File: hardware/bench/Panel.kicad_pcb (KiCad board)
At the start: 4 copper layers, 151 x 139 mm, 390 parts

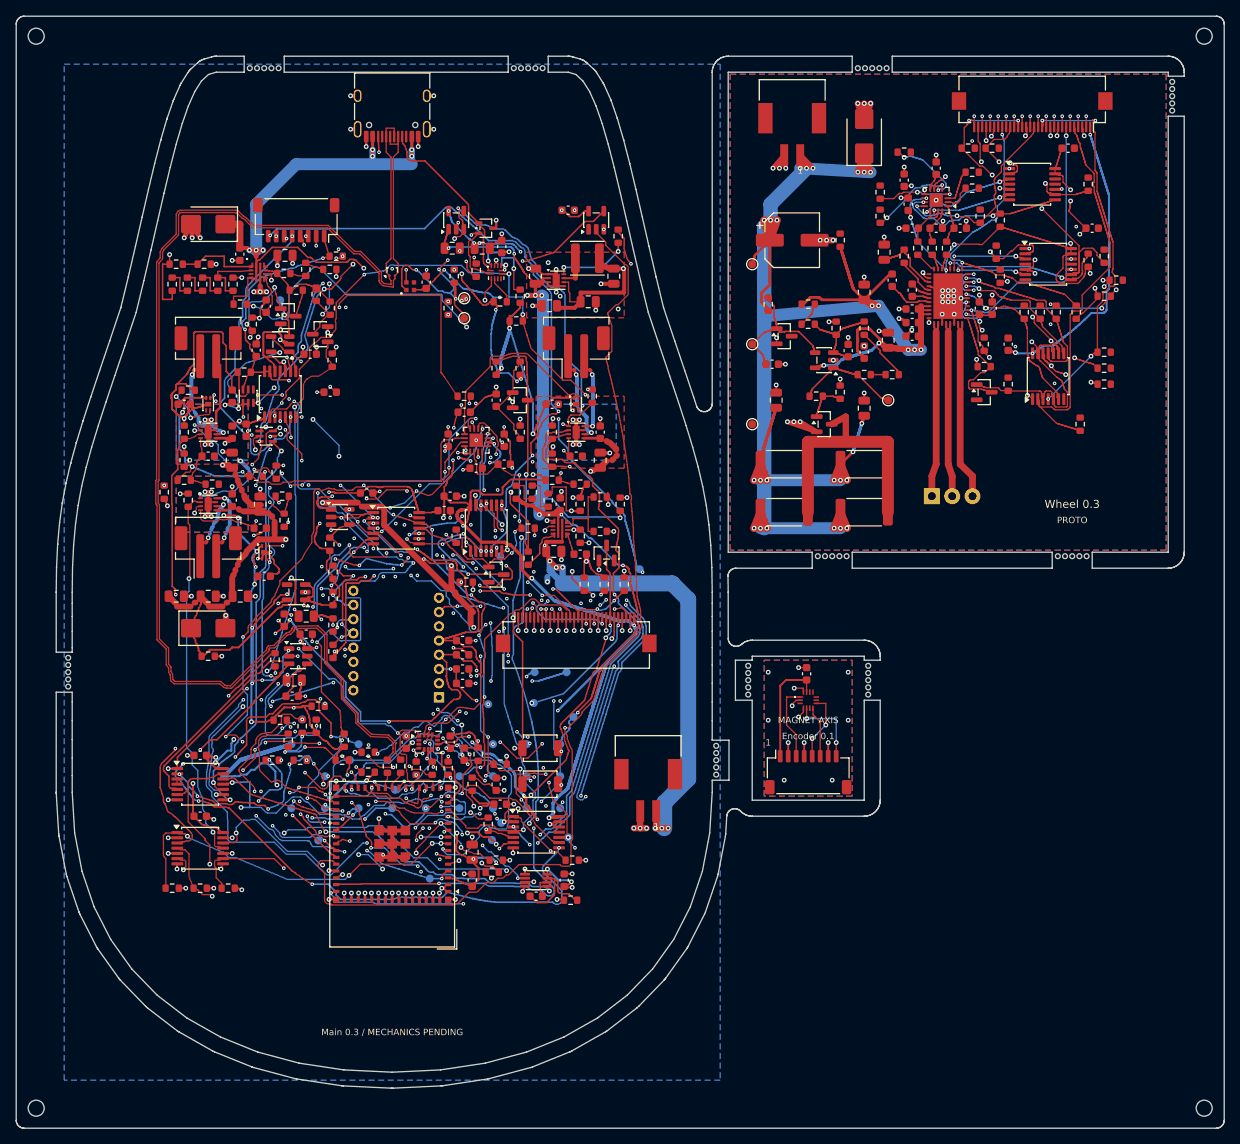
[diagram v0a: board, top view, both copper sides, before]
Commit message: Prepare wired Rev-A bench boards and submit manufacturing review
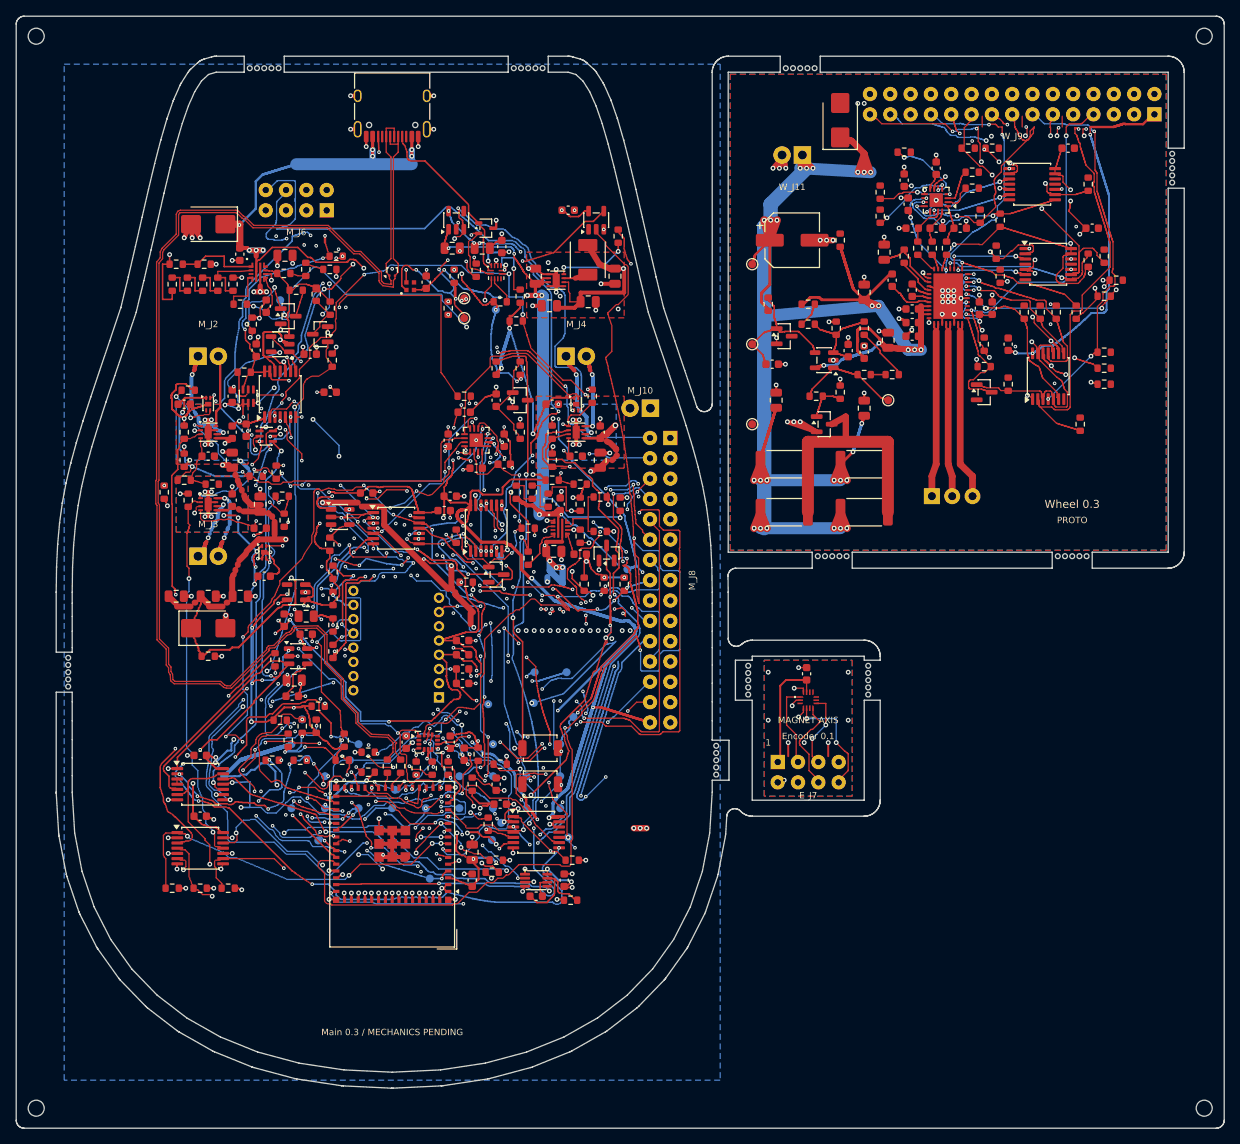
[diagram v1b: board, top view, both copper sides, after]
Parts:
- E_J7, M_J6: value ENCODER_8P -> Soldered wires Signal_2x04; footprint Connector_JST:JST_SH_SM08B-SRSS-TB_1x08-1MP_P1.00mm_Horizontal -> MagMouseModular:Wire_Signal_2x04_P2.54mm
- M_J10, W_J11: value WHEEL_POWER_2P -> Soldered wires Power_1x02; footprint MagMouseModular:JST_PA_SM02B-PASS_1x02_P2.00mm_Horizontal -> MagMouseModular:Wire_Power_1x02_P2.54mm
- M_J2: value COIL_L -> Soldered wires Power_1x02; footprint Connector_JST:JST_PH_B2B-PH-SM4-TB_1x02-1MP_P2.00mm_Vertical -> MagMouseModular:Wire_Power_1x02_P2.54mm
- M_J3: value COIL_M -> Soldered wires Power_1x02; footprint Connector_JST:JST_PH_B2B-PH-SM4-TB_1x02-1MP_P2.00mm_Vertical -> MagMouseModular:Wire_Power_1x02_P2.54mm
- M_J4: value COIL_R -> Soldered wires Power_1x02; footprint Connector_JST:JST_PH_B2B-PH-SM4-TB_1x02-1MP_P2.00mm_Vertical -> MagMouseModular:Wire_Power_1x02_P2.54mm
- M_J8, W_J9: value WHEEL_SIGNAL_30P -> Soldered wires Signal_2x15; footprint Connector_FFC-FPC:Hirose_FH12-30S-0.5SH_1x30-1MP_P0.50mm_Horizontal -> MagMouseModular:Wire_Signal_2x15_P2.54mm
- M_L1: value SWPA4020S3R3MT -> SRP4020CC-3R3M; footprint Inductor_SMD:L_Sunlord_SWPA4020S -> MagMouseModular:L_Bourns_SRP4020CC
- moved M_TP10 54.4 mm to (60.0, 36.7)
- moved M_J10 49.0 mm to (78.0, 49.0), turned to 180 degrees
- moved M_J8 12.3 mm to (80.5, 70.5), turned to -90 degrees
- moved MB6_1 9.00 mm to (144.5, 17.2)
- moved MB6_2 9.00 mm to (144.5, 18.1)
- moved MB5_1 9.00 mm to (96.2, 6.50)
- moved MB5_2 9.00 mm to (97.1, 6.50)
- moved MB5_3 9.00 mm to (98.0, 6.50)
- moved MB5_4 9.00 mm to (98.9, 6.50)
- moved MB5_5 9.00 mm to (99.8, 6.50)
- moved MB6_3 9.00 mm to (144.5, 19.0)
- moved MB6_5 9.00 mm to (144.5, 20.8)
- moved MB6_4 9.00 mm to (144.5, 19.9)
- moved W_D6 3.61 mm to (103.0, 13.0)
- moved W_J9 2.69 mm to (124.5, 11.0)
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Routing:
- net Main/WHEEL_PWM_B: track 54.4 -> 137.0 mm, vias 8 -> 10
- net Main/MOTOR_SPI_SCLK: track 67.3 -> 127.0 mm, vias 7 -> 11
- net Main/WHEEL_PWM_A: track 52.9 -> 108.3 mm, vias 8 -> 11
- net Main/CC_OUT1: track 127.2 -> 174.8 mm, vias 9 -> 11
- net Main/ACT_5V: track 244.2 -> 200.7 mm, vias 19 -> 17
- net Main/GND: track 310.8 -> 269.0 mm, vias 254 -> 259
- net Main/WHEEL_RUN_REQ: track 53.2 -> 94.8 mm, vias 5 -> 9
- net Main/RGB_DATA: track 143.8 -> 179.0 mm, vias 3 -> 5
- net Main/SPI_SCLK: track 92.6 -> 126.1 mm, vias 9 -> 10
- net Main/MOTOR_SPI_MOSI: track 52.1 -> 85.0 mm, vias 6 -> 11
- net Main/VBUS_USB: track 177.1 -> 148.2 mm
- net Main/CS_DRV8316: track 98.1 -> 126.6 mm, vias 12 -> 15
- net Main/SPI_MOSI: track 164.2 -> 192.6 mm, vias 15 -> 16
- net Main/DRV_FAULT_LOCAL_N: track 22.0 -> 46.4 mm, vias 5 -> 9
- net Main/WHEEL_PWM_C: track 66.3 -> 43.7 mm, vias 7 -> 4
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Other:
- outline, holes or cut-outs redrawn
